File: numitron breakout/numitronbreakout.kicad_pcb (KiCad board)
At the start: 4 copper layers, 60 x 100 mm, 17 parts, among them J1 Conn_01x06, M3 SCREW MountingHole_3.2mm_M3_Pad, U1 HV5812WG-G, U2 LM317_TO-220, U3 LM317_TO-220, U4 IV-12, U5 IV-12

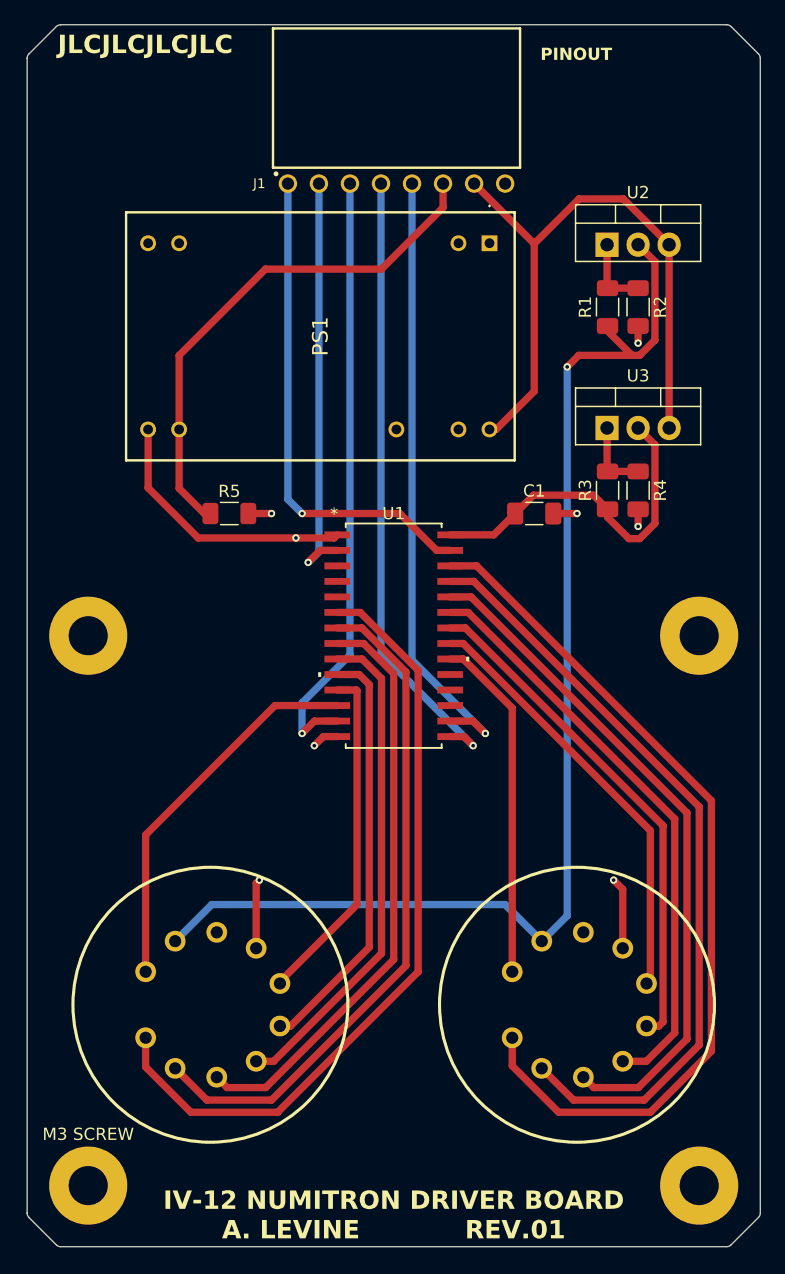
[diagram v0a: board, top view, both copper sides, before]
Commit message: updated trace widths and did some renders
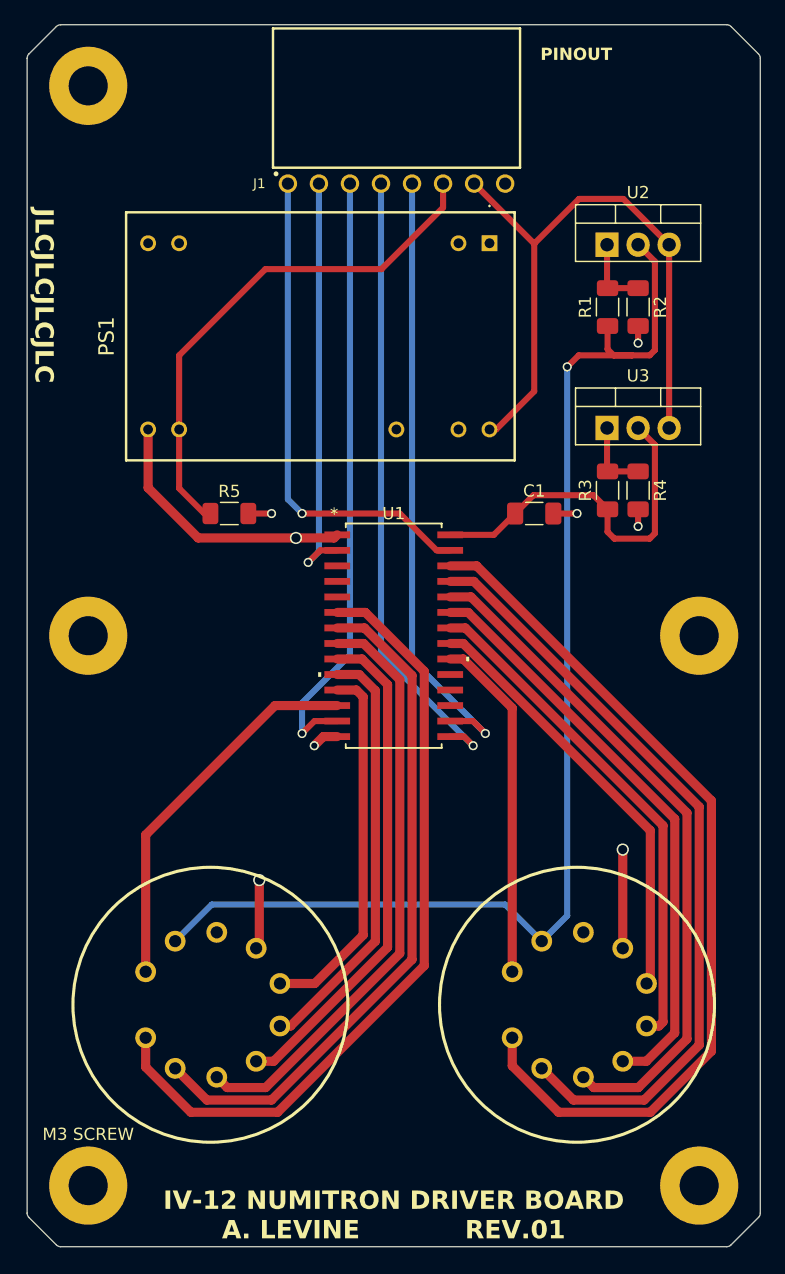
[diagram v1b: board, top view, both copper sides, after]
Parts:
- added REF**: MountingHole_3.2mm_M3_Pad, MountingHole:MountingHole_3.2mm_M3_Pad, F.Cu at (125.0, 100.0)
- moved REF** 45.0 mm to (125.0, 55.0)
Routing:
- net +30V: track 91.9 -> 96.5 mm
- net Net-(U1-HVOUT12): track 29.0 -> 31.1 mm
- net +1V5: track 100.0 -> 101.4 mm
- net +5V: track 28.8 -> 30.0 mm
- net Net-(U1-HVOUT17): track 64.2 -> 64.9 mm
- net Net-(U1-HVOUT16): track 55.7 -> 56.2 mm

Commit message: minor pcb layout updates
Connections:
- REF** pad 1: (no net) -> GND
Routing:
- net +30V: track 96.5 -> 96.8 mm, vias 3 -> 1
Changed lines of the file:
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@@
 	(net 36 "unconnected-(PS1--VOUT_2-Pad12)")
 	(net 37 "unconnected-(PS1--VIN_2-Pad2)")
+	(footprint "MountingHole:MountingHole_3.2mm_M3_Pad"
+		(layer "F.Cu")
+		(at 125 100)
+		(descr "Mounting Hole 3.2mm, M3")
+		(tags "mounting hole 3.2mm m3")
+		(property "Reference" "REF**"
+			(at 0 -4.2 0)
+			(layer "F.SilkS")
+			(hide yes)
+			(effects
+				(font
+					(size 1 1)
+					(thickness 0.15)
+				)
+			)
+		)
+		(property "Value" "MountingHole_3.2mm_M3_Pad"
+			(at 0 4.2 0)
+			(layer "F.Fab")
+			(effects
+				(font
+					(size 1 1)
+					(thickness 0.15)
+				)
+			)
+		)
+		(property "Footprint" "MountingHole:MountingHole_3.2mm_M3_Pad"
+			(at 0 0 0)
+			(unlocked yes)
+			(layer "F.Fab")
+			(hide yes)
+			(effects
+				(font
+					(size 1.27 1.27)
+					(thickness 0.15)
+				)
+			)
+		)
+		(property "Datasheet" ""
+			(at 0 0 0)
+			(unlocked yes)
+			(layer "F.Fab")
+			(hide yes)
+			(effects
+				(font
+					(size 1.27 1.27)
+					(thickness 0.15)
+				)
+			)
+		)
+		(property "Description" ""
+			(at 0 0 0)
+			(unlocked yes)
+			(layer "F.Fab")
+			(hide yes)
+			(effects
+				(font
+					(size 1.27 1.27)
+					(thickness 0.15)
+				)
+			)
+		)
+		(attr exclude_from_pos_files exclude_from_bom)
+		(fp_circle
+			(center 0 0)
+			(end 3.2 0)
+			(stroke
+				(width 0.15)
+				(type solid)
+			)
+			(fill none)
+			(layer "Cmts.User")
+		)
+		(fp_circle
+			(center 0 0)
+			(end 3.45 0)
+			(stroke
+				(width 0.05)
+				(type solid)
+			)
+			(fill none)
+			(layer "F.CrtYd")
+		)
+		(fp_text user "${REFERENCE}"
+			(at 0 0 0)
+			(layer "F.Fab")
+			(effects
+				(font
+					(size 1 1)
+					(thickness 0.15)
+				)
+			)
+		)
+		(pad "1" thru_hole circle
+			(at 0 0)
+			(size 6.4 6.4)
+			(drill 3.2)
+			(layers "*.Cu" "*.Mask")
+			(remove_unused_layers no)
+			(net 31 "GND")
+			(thermal_bridge_width 1)
+		)
+	)
 	(footprint "NewFootprints:iv-12"
 		(layer "F.Cu")
@@
 		)
 		(fp_text user "*"
-			(at -4.8768 -9.9568 0)
-			(unlocked yes)
-			(layer "F.SilkS")
-			(effects
-				(font
-					(size 1 1)
-					(thickness 0.15)
-				)
-			)
-		)
-		(fp_text user "*"
-			(at -4.8768 -9.9568 0)
-			(layer "F.SilkS")
-			(effects
-				(font
-					(size 1 1)
-					(thickness 0.15)
-				)
-			)
-		)
-		(fp_text user "*"
 			(at -3.4163 -8.9789 0)
 			(layer "F.Fab")
@@
 		)
 	)
-	(footprint "MountingHole:MountingHole_3.2mm_M3_Pad"
-		(layer "F.Cu")
-		(at 125 100)
-		(descr "Mounting Hole 3.2mm, M3")
-		(tags "mounting hole 3.2mm m3")
-		(property "Reference" "REF**"
-			(at 0 -4.2 0)
-			(layer "F.SilkS")
-			(hide yes)
-			(effects
-				(font
-					(size 1 1)
-					(thickness 0.15)
-				)
-			)
-		)
-		(property "Value" "MountingHole_3.2mm_M3_Pad"
-			(at 0 4.2 0)
-			(layer "F.Fab")
-			(effects
-				(font
-					(size 1 1)
-					(thickness 0.15)
-				)
-			)
-		)
-		(property "Footprint" "MountingHole:MountingHole_3.2mm_M3_Pad"
-			(at 0 0 0)
-			(unlocked yes)
-			(layer "F.Fab")
-			(hide yes)
-			(effects
-				(font
-					(size 1.27 1.27)
-					(thickness 0.15)
-				)
-			)
-		)
-		(property "Datasheet" ""
-			(at 0 0 0)
-			(unlocked yes)
-			(layer "F.Fab")
-			(hide yes)
-			(effects
-				(font
-					(size 1.27 1.27)
-					(thickness 0.15)
-				)
-			)
-		)
-		(property "Description" ""
-			(at 0 0 0)
-			(unlocked yes)
-			(layer "F.Fab")
-			(hide yes)
-			(effects
-				(font
-					(size 1.27 1.27)
-					(thickness 0.15)
-				)
-			)
-		)
-		(attr exclude_from_pos_files exclude_from_bom)
-		(fp_circle
-			(center 0 0)
-			(end 3.2 0)
-			(stroke
-				(width 0.15)
-				(type solid)
-			)
-			(fill none)
-			(layer "Cmts.User")
-		)
-		(fp_circle
-			(center 0 0)
-			(end 3.45 0)
-			(stroke
-				(width 0.05)
-				(type solid)
-			)
-			(fill none)
-			(layer "F.CrtYd")
-		)
-		(fp_text user "${REFERENCE}"
-			(at 0 0 0)
-			(layer "F.Fab")
-			(effects
-				(font
-					(size 1 1)
-					(thickness 0.15)
-				)
-			)
-		)
-		(pad "1" thru_hole circle
-			(at 0 0)
-			(size 6.4 6.4)
-			(drill 3.2)
-			(layers "*.Cu" "*.Mask")
-			(remove_unused_layers no)
-			(thermal_bridge_width 1)
-			(thermal_bridge_angle 22.5)
-		)
-	)
 	(footprint "Resistor_SMD:R_1206_3216Metric_Pad1.30x1.75mm_HandSolder"
 		(layer "F.Cu")
@@
 	)
 	(segment
-		(start 139 120)
-		(end 139 125.3209)
-		(width 0.75)
-		(layer "F.Cu")
-		(net 1)
-	)
-	(segment
-		(start 168.744 117.5)
-		(end 168.744 125.5769)
-		(width 0.75)
-		(layer "F.Cu")
-		(net 1)
-	)
-	(segment
 		(start 129.9 83.12)
 		(end 129.9 87.9)
@@
 	)
 	(segment
-		(start 139 125.3209)
-		(end 138.744 125.5769)
+		(start 142 92)
+		(end 145.1222 92)
 		(width 0.75)
 		(layer "F.Cu")
@@
 	)
 	(segment
-		(start 142 92)
-		(end 145.1222 92)
+		(start 145.1222 92)
+		(end 145.3772 91.745)
 		(width 0.75)
 		(layer "F.Cu")
@@
 	)
 	(segment
-		(start 145.1222 92)
-		(end 145.3772 91.745)
+		(start 139 125.3209)
+		(end 138.744 125.5769)
 		(width 0.75)
 		(layer "F.Cu")
@@
 	)
 	(via
-		(at 139 120)
-		(size 1)
-		(drill 0.75)
-		(layers "F.Cu" "B.Cu")
-		(net 1)
-	)
-	(via
-		(at 168.744 117.5)
-		(size 1)
-		(drill 0.75)
-		(layers "F.Cu" "B.Cu")
-		(net 1)
-	)
-	(via
 		(at 142 92)
 		(size 1)
@@
 	)
 	(segment
-		(start 139 120)
-		(end 139 117)
+		(start 139 95)
+		(end 142 92)
 		(width 0.75)
 		(layer "In2.Cu")
@@
 	)
 	(segment
-		(start 139 95)
-		(end 142 92)
+		(start 168.744 117.5)
+		(end 167.244 116)
 		(width 0.75)
 		(layer "In2.Cu")
@@
 	)
 	(segment
-		(start 168.744 117.5)
-		(end 167.244 116)
+		(start 141.5 116)
+		(end 139 113.5)
 		(width 0.75)
 		(layer "In2.Cu")
@@
 	)
 	(segment
-		(start 139 117)
+		(start 139 125.3209)
 		(end 139 95)
 		(width 0.75)
@@
 	)
 	(segment
-		(start 141.5 116)
-		(end 139 113.5)
+		(start 168.744 125.5769)
+		(end 168.744 117.5)
+		(width 0.75)
+		(layer "In2.Cu")
+		(net 1)
+	)
+	(segment
+		(start 138.744 125.5769)
+		(end 139 125.3209)
 		(width 0.75)
 		(layer "In2.Cu")
@@
 		(polygon
 			(pts
-				(xy 125 55) (xy 175 55) (xy 175 145) (xy 125 145)
+				(xy 121.5 55) (xy 125 51.5) (xy 175 51.5) (xy 178.5 55) (xy 178.5 145) (xy 175 148.5) (xy 125 148.5)
+				(xy 121.5 145)
 			)
 		)

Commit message: updated power supply
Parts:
- PS1: value LDB-500L -> LDB-350L
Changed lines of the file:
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@@
 			)
 		)
-		(property "Value" "LDB-500L"
+		(property "Value" "LDB-350L"
 			(at 7.62 13.84 90)
 			(layer "F.SilkS")
@@
 			)
 		)
-		(property "Description" "LED DVR CC BUCK-BST 2-32V 500MA"
+		(property "Description" "LED DVR CC BUCK-BST 2-40V 350MA"
 			(at 0 0 90)
 			(layer "F.Fab")
@@
 			)
 		)
-		(property "Description_1" "500mA 2 ~ 32V Constant Current LED Driver Buck-Boost Topology 1 Output"
+		(property "Description_1" "350mA 2 ~ 40V Constant Current LED Driver Buck-Boost Topology 1 Output"
 			(at 0 0 -90)
 			(unlocked yes)
